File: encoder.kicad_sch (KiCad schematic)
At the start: 11 parts, among them P1 Molex PicoBlade 6 Right, U1 TLE5012B

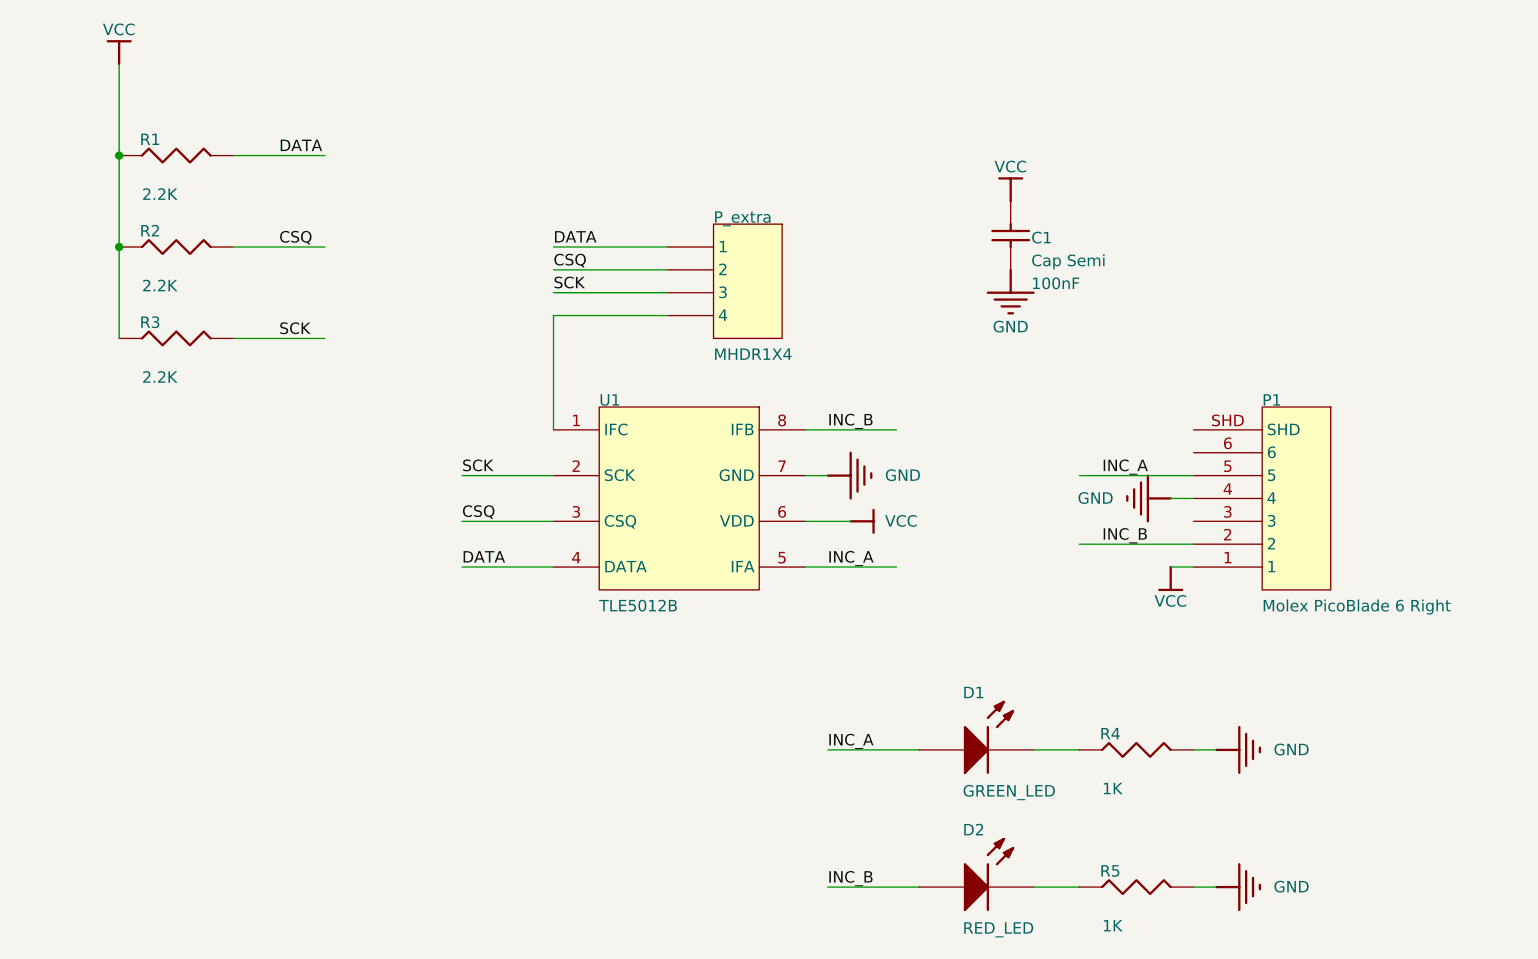
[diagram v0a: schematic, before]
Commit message: Move to kicad symbols, route INC_C to the main connector.
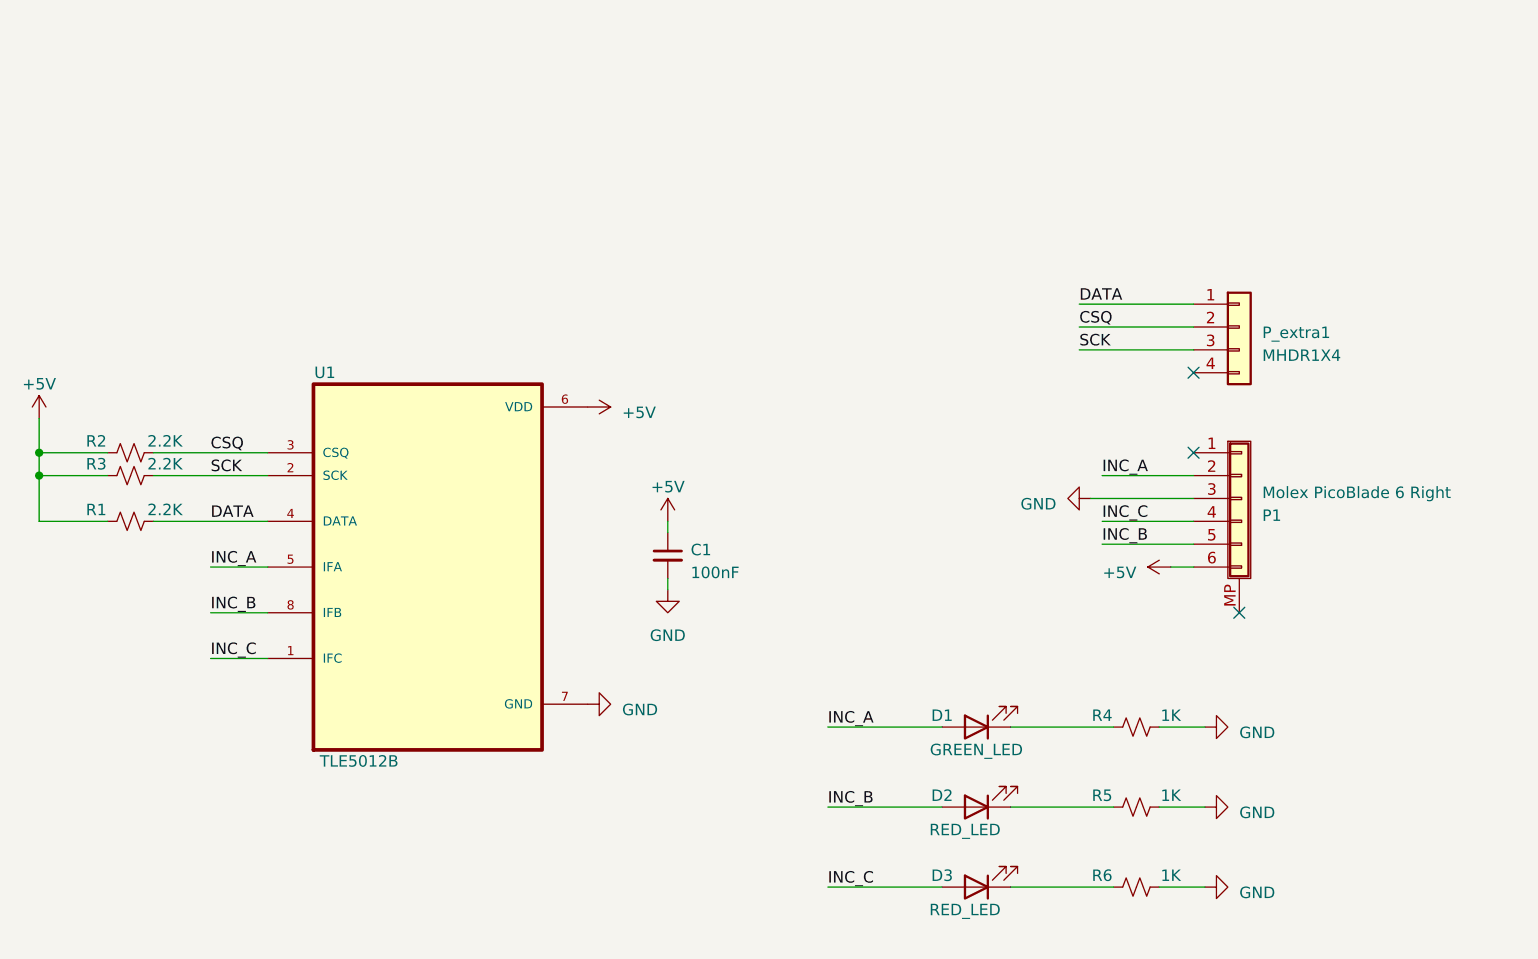
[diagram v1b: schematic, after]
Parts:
- removed C1: Cap Semi, 1608[0603], symbol encoder-altium-import:root_1_Cap Semi
- removed D1: GREEN_LED, 1608[0603], symbol encoder-altium-import:root_0_LED2
- removed D2: RED_LED, 1608[0603], symbol encoder-altium-import:root_0_LED2
- removed P1: Molex PicoBlade 6 Right, Molex PicoBlade 6 Right SMD, symbol encoder-altium-import:root_0_mirrored_Molex PicoBlade 6 Right
- removed P_extra: MHDR1X4, MHDR1X4, symbol encoder-altium-import:root_0_MHDR1X4
- removed R1, R2, R3, R4, R5: Res3, J1-0603, symbol encoder-altium-import:root_0_Res3
- removed U1: TLE5012B, SO-8, symbol encoder-altium-import:root_0_TLE5012B
- added C1: 100nF, Capacitor_SMD:C_0603_1608Metric_Pad1.08x0.95mm_HandSolder, symbol Device:C_Small
- added D1: GREEN_LED, LED_SMD:LED_0603_1608Metric_Pad1.05x0.95mm_HandSolder, symbol Device:LED
- added D2, D3: RED_LED, LED_SMD:LED_0603_1608Metric_Pad1.05x0.95mm_HandSolder, symbol Device:LED
- added P1: Molex PicoBlade 6 Right, 532610671:Molex_PicoBlade_53261-0671_1x06-1MP_P1.25mm_Horizontal, symbol conn_01x06_shielded:532610671
- added P_extra1: MHDR1X4, Connector_PinHeader_1.27mm:PinHeader_1x04_P1.27mm_Horizontal, symbol Connector_Generic:Conn_01x04
- added R1, R2, R3: 2.2K, Resistor_SMD:R_0603_1608Metric_Pad0.98x0.95mm_HandSolder, symbol Device:R_Small_US
- added R4, R5, R6: 1K, Resistor_SMD:R_0603_1608Metric_Pad0.98x0.95mm_HandSolder, symbol Device:R_Small_US
- added U1: TLE5012B, TLE5012BE9000XUMA1:SOIC127P600X175-8N, symbol TLE5012BE9000XUMA1:TLE5012BE9000XUMA1
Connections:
- net CSQ: now also P_extra1.2 (Pin_2), R2.2, U1.3 (CSQ)
- net DATA: now also P_extra1.1 (Pin_1), R1.2, U1.4 (DATA)
- net GND: now also C1.2, P1.3 (Pin_3), R4.2, R5.2, R6.2, U1.7 (GND)
- net INC_A: now also D1.2 (A), P1.2 (Pin_2), U1.5 (IFA)
- net INC_B: now also D2.2 (A), P1.5 (Pin_5), U1.8 (IFB)
- net SCK: now also P_extra1.3 (Pin_3), R3.2, U1.2 (SCK)
- new net: D2.1 (K), R5.1
- new net: D1.1 (K), R4.1
- new net: D3.1 (K), R6.1
- new net +5V: C1.1, P1.6 (Pin_6), R1.1, R2.1, R3.1, U1.6 (VDD)
- new net INC_C: D3.2 (A), P1.4 (Pin_4), U1.1 (IFC)
- no-connect marks 0 -> 3
